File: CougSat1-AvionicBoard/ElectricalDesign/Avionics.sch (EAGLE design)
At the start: 164 parts, among them J11 -Y, J12 +Z, J13 +X, J14 -Z, J15 +Y, J3 SWD, J4 CougSat Card, J5 -X, J8 SWD, J9 SWD, U1 STM32L476RGT, U10 BNO055, U11 128KB, U12 TXS0102DQM, U13 TXS0102DQM, U14 LTC2499, U15 BNO055, U16 BNO055, U17 TXS0102DQM, U18 TXS0102DQM, U2 STM32L476RGT, U3 STM32L476RGT, U4 128KB, U5 DRV8837, U6 DRV8837, U7 DRV8837, U8 LTC2499, U9 Venus838FLPx-L, Y1 16MHz ±10ppm, Y10 16MHz ±10ppm, Y2 32.768kHz ±10ppm, Y3 16MHz ±10ppm, Y4 32.768kHz ±10ppm, Y6 32.768kHz ±10ppm, Y7 32.768kHz ±10ppm, Y8 32.768kHz ±10ppm, Y9 32.768kHz ±10ppm

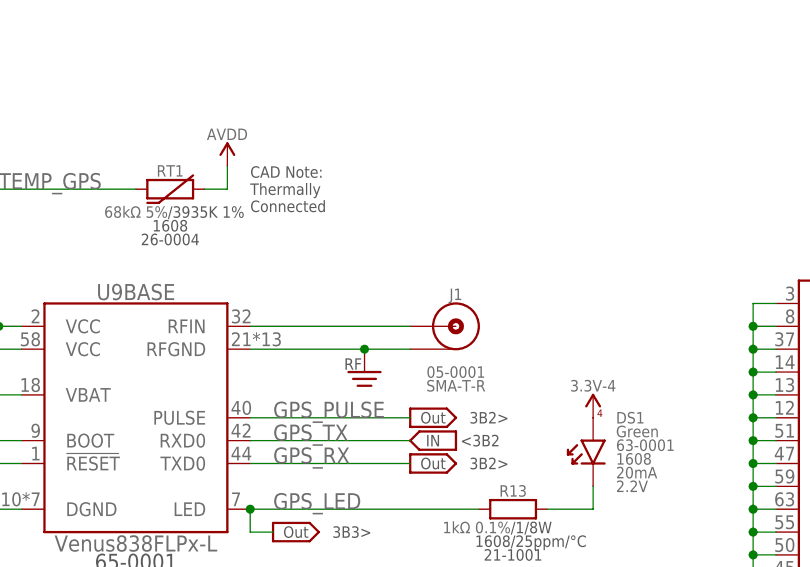
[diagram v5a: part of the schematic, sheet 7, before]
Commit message: Added inductor
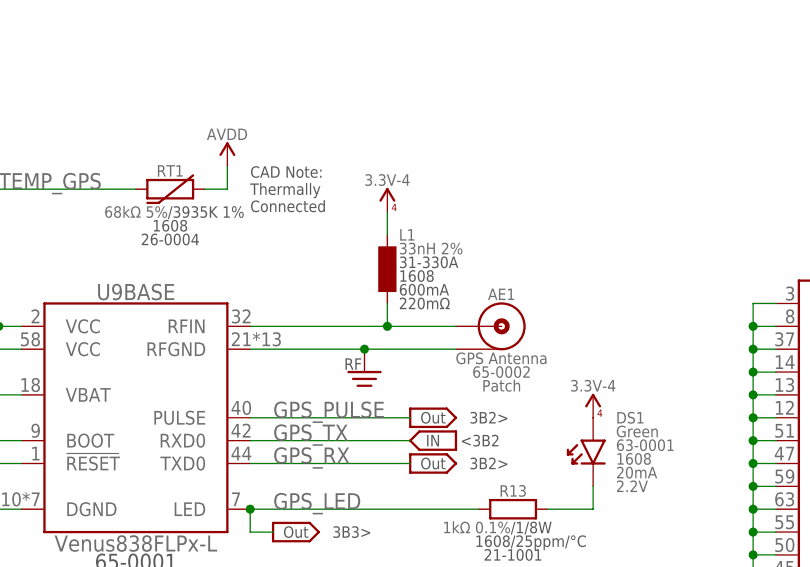
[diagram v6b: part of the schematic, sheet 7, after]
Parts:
- removed J1: (no value), CougsInSpace-Connectors:COAX-SMA-T-R
- added AE1: GPS Antenna, CougsInSpace-RF:ANTENNA-GPSPATCH
- added L1: 33nH 2%, CougsInSpace-Coils:INDUCTOR-V-33NH-1608
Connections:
- net 3.3V_4: now also L1.2
- net AGND: now also AE1.SHIELD; no longer J1.SHIELD
- net N$17: now also AE1.CENTER, L1.1; no longer J1.CENTER
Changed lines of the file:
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@@
 <part name="C15" library="CougsInSpace-Capacitors" deviceset="CAP-V" device="-1608" technology="-1UF" value="1µF 10%"/>
 <part name="SUPPLY65" library="CougsInSpace-PowerSymbols" deviceset="DGND" device=""/>
-<part name="J1" library="CougsInSpace-Connectors" deviceset="COAX" device="-SMA-T-R"/>
 <part name="SUPPLY66" library="CougsInSpace-PowerSymbols" deviceset="DGND" device=""/>
 <part name="SUPPLY67" library="CougsInSpace-PowerSymbols" deviceset="DGND" device=""/>
@@
 <part name="DS5" library="CougsInSpace-LEDs" deviceset="LED-H" device="-1608" technology="-GRN" value="Green"/>
 <part name="DS3" library="CougsInSpace-LEDs" deviceset="LED-H" device="-1608" technology="-YLW" value="Yellow"/>
+<part name="AE1" library="CougsInSpace-RF" deviceset="ANTENNA" device="-GPSPATCH" value="GPS Antenna"/>
+<part name="L1" library="CougsInSpace-Coils" deviceset="INDUCTOR-V" device="-1608" technology="-33NH" value="33nH 2%"/>
+<part name="SUPPLY178" library="CougsInSpace-PowerSymbols" deviceset="3.3V-4" device=""/>
 </parts>
 <sheets>
@@
 <instance part="C15" gate="G$1" x="76.2" y="63.5"/>
 <instance part="SUPPLY65" gate="1" x="76.2" y="58.42"/>
-<instance part="J1" gate="G$1" x="124.46" y="119.38"/>
 <instance part="SUPPLY66" gate="1" x="193.04" y="86.36"/>
 <instance part="SUPPLY67" gate="1" x="157.48" y="83.82"/>
@@
 <instance part="SUPPLY60" gate="G$1" x="22.86" y="149.86"/>
 <instance part="C10" gate="G$1" x="38.1" y="96.52"/>
+<instance part="AE1" gate="G$1" x="129.54" y="119.38"/>
+<instance part="L1" gate="G$1" x="116.84" y="124.46"/>
+<instance part="SUPPLY178" gate="G$1" x="116.84" y="132.08"/>
 </instances>
 <busses>
@@
 <segment>
 <pinref part="U9" gate="BASE" pin="RFIN"/>
-<wire x1="101.6" y1="119.38" x2="119.38" y2="119.38" width="0.1524" layer="91"/>
-<pinref part="J1" gate="G$1" pin="CENTER"/>
+<wire x1="101.6" y1="119.38" x2="116.84" y2="119.38" width="0.1524" layer="91"/>
+<pinref part="AE1" gate="G$1" pin="CENTER"/>
+<pinref part="L1" gate="G$1" pin="1"/>
+<wire x1="116.84" y1="119.38" x2="124.46" y2="119.38" width="0.1524" layer="91"/>
+<wire x1="116.84" y1="121.92" x2="116.84" y2="119.38" width="0.1524" layer="91"/>
+<junction x="116.84" y="119.38"/>
 </segment>
 </net>
@@
 <wire x1="101.6" y1="116.84" x2="114.3" y2="116.84" width="0.1524" layer="91"/>
 <pinref part="SUPPLY57" gate="G$1" pin="RFGND"/>
-<wire x1="114.3" y1="116.84" x2="119.38" y2="116.84" width="0.1524" layer="91"/>
+<wire x1="114.3" y1="116.84" x2="124.46" y2="116.84" width="0.1524" layer="91"/>
 <junction x="114.3" y="116.84"/>
-<pinref part="J1" gate="G$1" pin="SHIELD"/>
+<pinref part="AE1" gate="G$1" pin="SHIELD"/>
 </segment>
 </net>
@@
 <junction x="22.86" y="149.86"/>
 </segment>
+<segment>
+<pinref part="L1" gate="G$1" pin="2"/>
+<wire x1="116.84" y1="129.54" x2="116.84" y2="132.08" width="0.1524" layer="91"/>
+<pinref part="SUPPLY178" gate="G$1" pin="3.3V_4"/>
+</segment>
 </net>

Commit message: Updated Thermistors
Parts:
- removed RT12, RT13, RT14: 68kΩ 5%, CougsInSpace-Resistors:THERMISTOR-H-68K-1608
- added R47, R48, R49, R50, R51, R52, R53, R54, R55, R56, R57, R58, R59, R60: 10kΩ 0.1%, CougsInSpace-Resistors:RES-V-10K-1608
- added RT15, RT16, RT17, RT18: 10kΩ 5%, CougsInSpace-Resistors:THERMISTOR-V-10K-1608
- RT1, RT10, RT2, RT3, RT4, RT5, RT6, RT7, RT8, RT9: value 68kΩ 5% -> 10kΩ 5%; device CougsInSpace-Resistors:THERMISTOR-H-68K-1608 -> CougsInSpace-Resistors:THERMISTOR-V-10K-1608
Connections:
- net AGND: now also RT1.1, RT10.1, RT15.1, RT16.1, RT17.1, RT18.1, RT2.1, RT3.1, RT4.1, RT5.1, RT6.1, RT7.1, RT8.1, RT9.1
- net AVDD: no longer RT1.2, RT10.2, RT12.2, RT13.2, RT14.2, RT2.2, RT3.2, RT4.2, RT5.2, RT6.2, RT7.2, RT8.2, RT9.2
- net AVREF: now also R47.2, R48.2, R49.2, R50.2, R51.2, R52.2, R53.2, R54.2, R55.2, R56.2, R57.2, R58.2, R59.2, R60.2
- net TEMP_ADCS: now also R47.1, RT15.2
- net TEMP_GPS: now also R54.1, RT1.2; no longer RT1.1
- net TEMP_H-BRIDGE-X: now also R51.1, R59.1, R60.1, RT6.2, RT7.2, RT8.2; no longer RT3.1
- net TEMP_H-BRIDGE-Y: now also R52.1, RT9.2; no longer RT4.1
- net TEMP_H-BRIDGE-Z: now also R53.1, RT10.2; no longer RT5.1
- net TEMP_IFJR: now also R55.1, RT3.2; no longer RT2.1
- net TEMP_IHU: now also R58.1, RT5.2; no longer RT14.1
- net TEMP_IMU0: now also R48.1, RT16.2; no longer RT8.1
- net TEMP_IMU1: now also R49.1, RT17.2; no longer RT9.1
- net TEMP_IMU2: now also R50.1, RT18.2; no longer RT10.1
- net TEMP_SD_IFJR0: now also R56.1, RT2.2; no longer RT6.1
- net TEMP_SD_IFJR1: now also R57.1, RT4.2; no longer RT7.1
- net TEMP_SD_IHU0: no longer RT12.1
- net TEMP_SD_IHU1: no longer RT13.1
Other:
- note added: "4A5>"
- note added: "6A2>"
- note added: "6A4>"
- note added: "<3A6"
- note added: "<4A5"
- note added: "<4A6"
- note added: "<5A6"
- note added: "<5B6"
- note added: "<5C6"
- note removed: "<3A5"
- note removed: "<4A1"
- note removed: "<5B2"
- note removed: "<5C2"
- note removed: "<5D2"
- note removed: "<6A2"
- note removed: "<6A4"
- note removed: "<6B2"
- note removed: "<6C2"
- moved on the sheet: C25, C26, DS3, DS5, J2, J6, J9, R25, R27, R38, R44, R46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

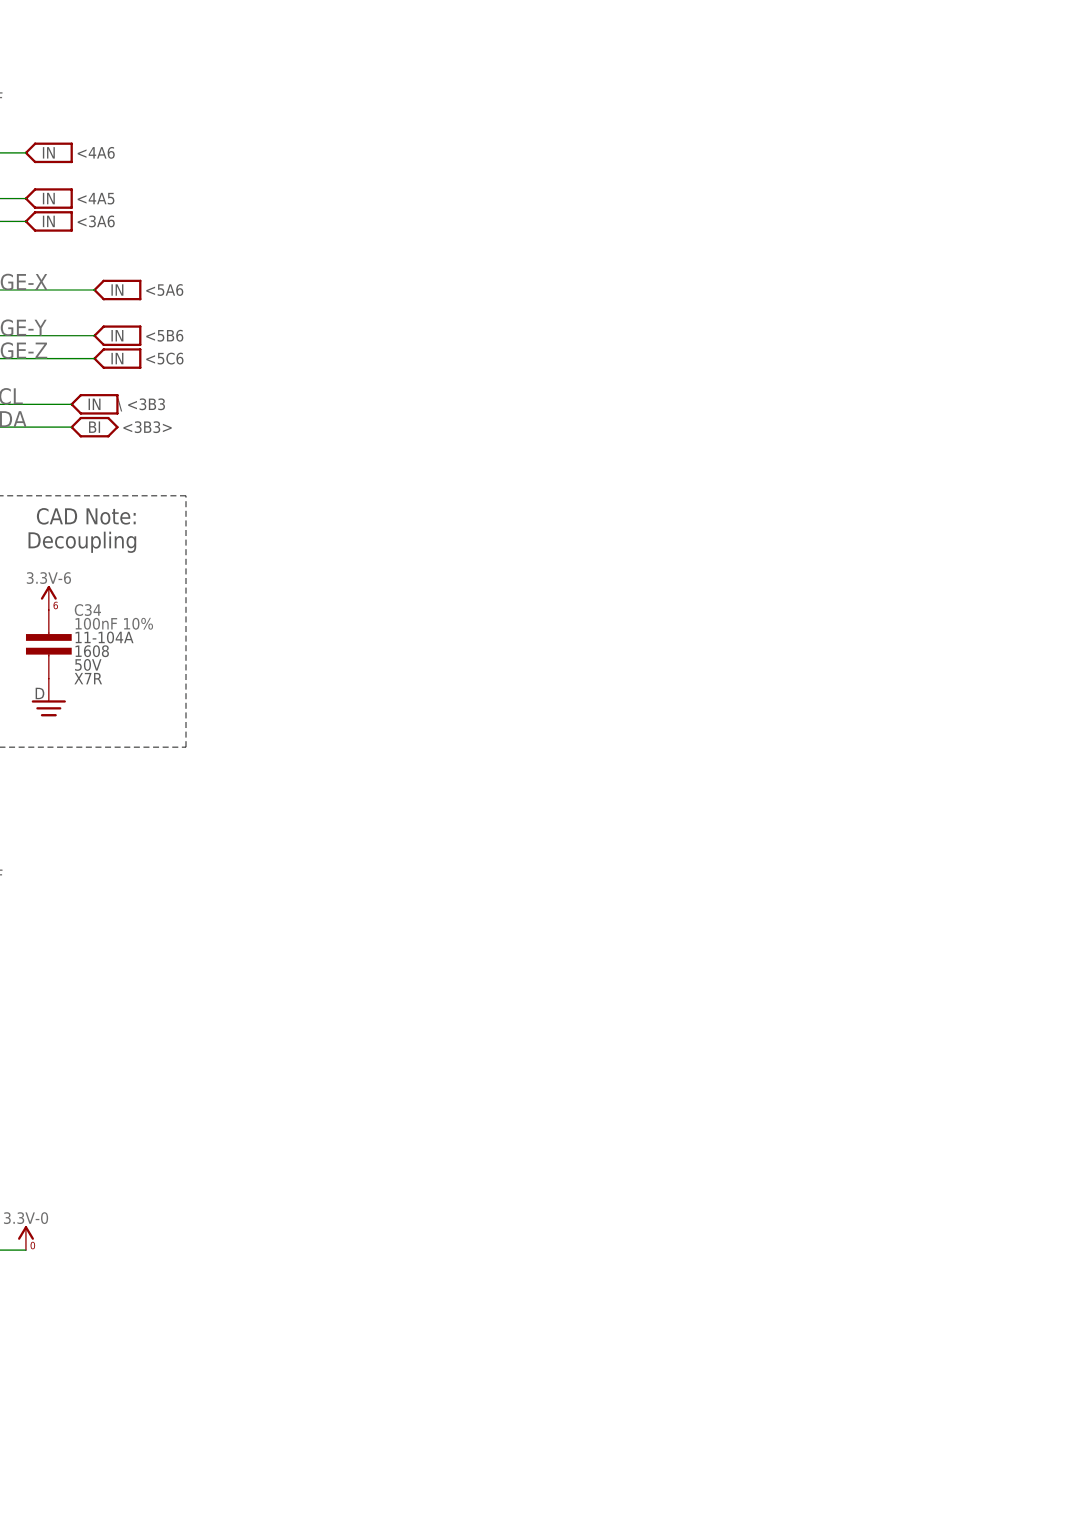
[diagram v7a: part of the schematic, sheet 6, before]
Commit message: Added Current-Sense Amplifiers
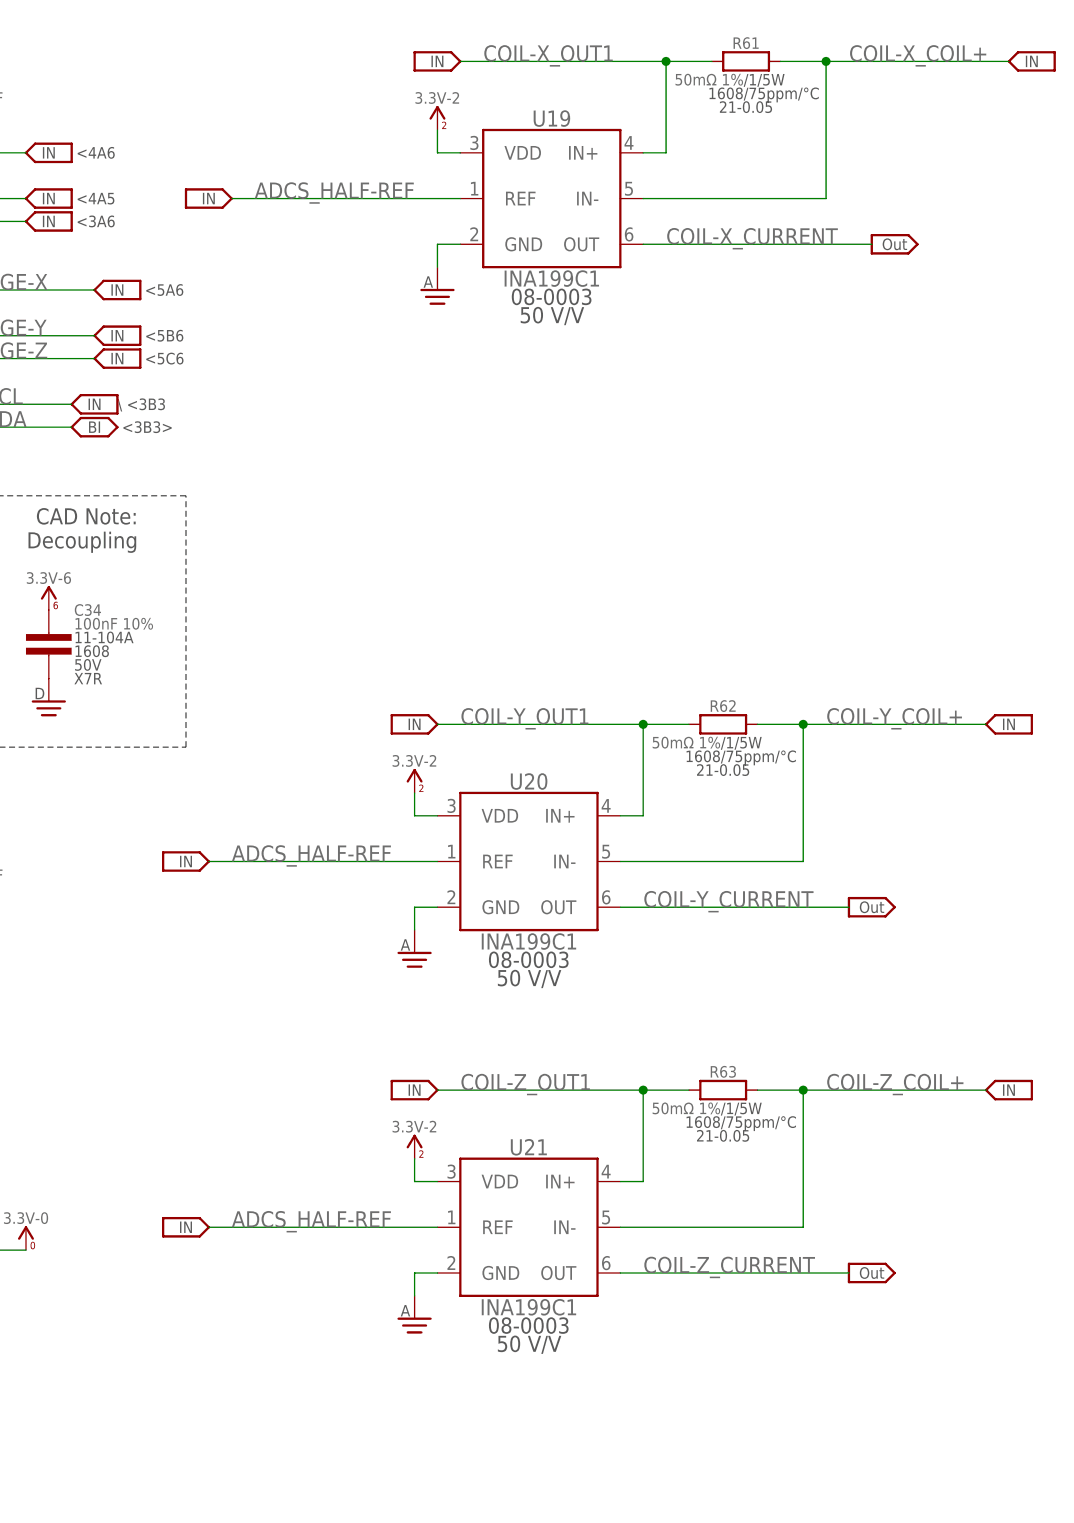
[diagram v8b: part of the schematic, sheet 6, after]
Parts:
- added R61, R62, R63: 50mΩ 1%, CougsInSpace-Resistors:RES-H-0.05R-1608
- added U19, U20, U21: INA199C1, CougsInSpace-IC-Amplifiers:INA199C1
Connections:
- new net ADCS_HALF-REF: U19.REF, U20.REF, U21.REF
- new net COIL-X_CURRENT: U19.OUT
- new net COIL-Y_CURRENT: U20.OUT
- new net COIL-Z_CURRENT: U21.OUT
- net 3.3V_2: now also U19.VDD, U20.VDD, U21.VDD
- net AGND: now also U19.GND, U20.GND, U21.GND
- net COIL-X_COIL+: now also R61.2, U19.IN-
- net COIL-X_OUT1: now also R61.1, U19.IN+
- net COIL-Y_COIL+: now also R62.2, U20.IN-
- net COIL-Y_OUT1: now also R62.1, U20.IN+
- net COIL-Z_COIL+: now also R63.2, U21.IN-
- net COIL-Z_OUT1: now also R63.1, U21.IN+
